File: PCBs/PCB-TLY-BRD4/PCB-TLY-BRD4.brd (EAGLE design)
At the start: 100 x 31 mm, 28 parts, among them IC1 ULN2803A, IC2 MCP23017SS

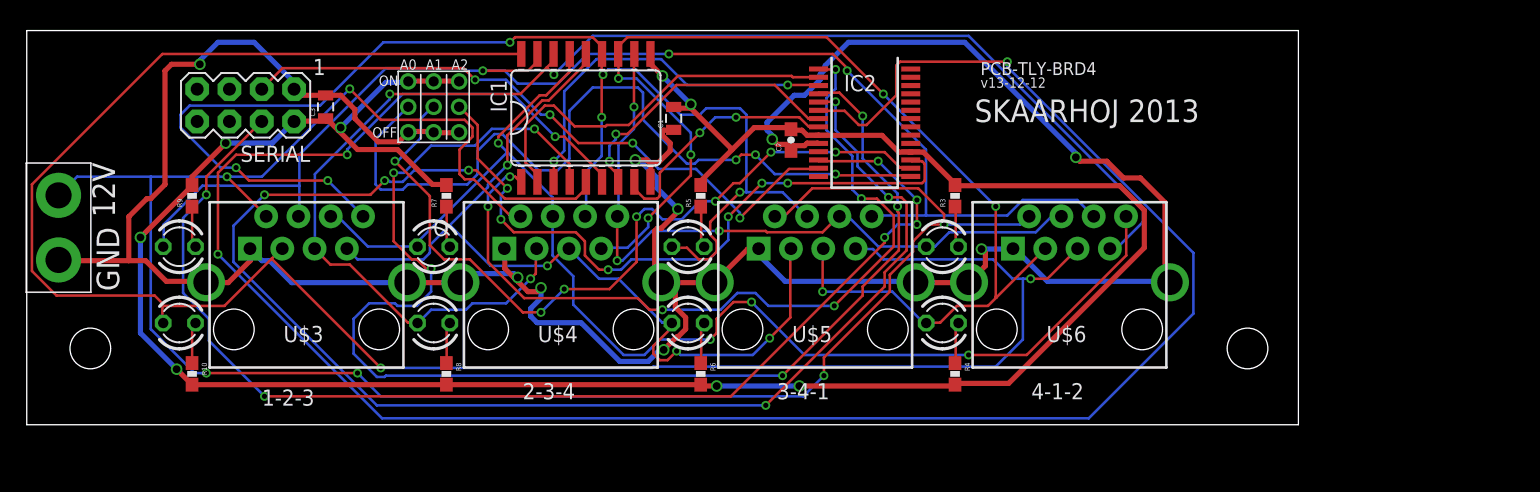
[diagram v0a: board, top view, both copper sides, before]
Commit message: Updated boards
Updated boards with logo before first sending to Alma.
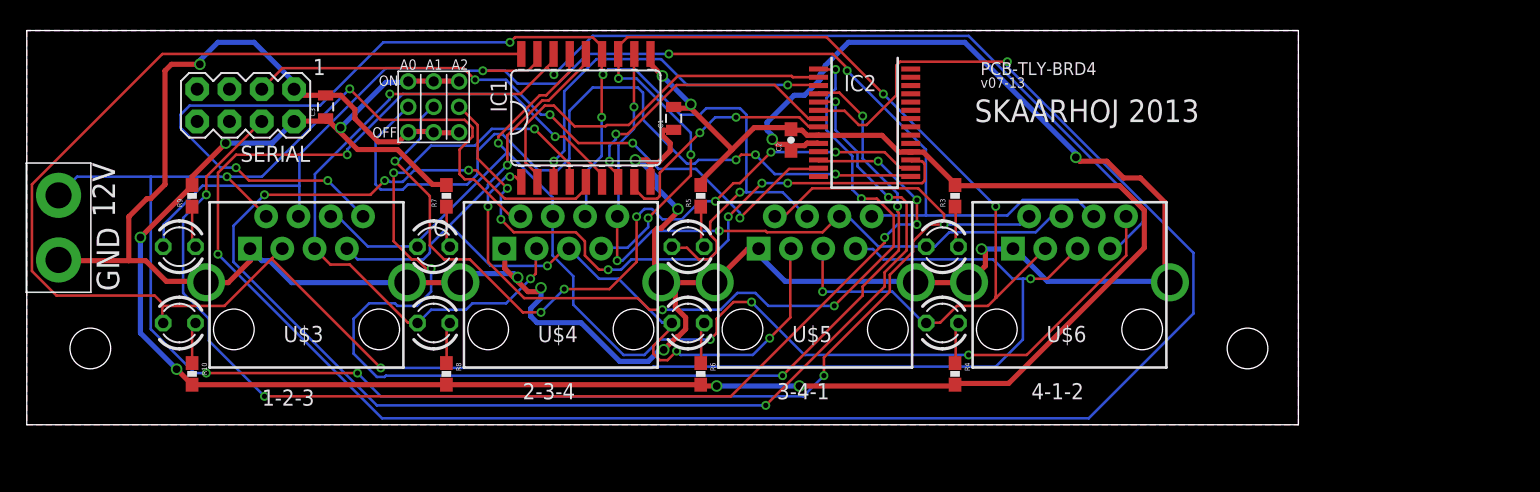
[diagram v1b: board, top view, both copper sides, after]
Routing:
- added copper zone on layer 1, net GND
- added copper zone on layer 16, net GND
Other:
- board text added: "v07-13"
- board text removed: "v13-12-12"

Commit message: Some new stuff
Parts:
- removed JP1: (no value), SparkFun:1X02_XTRA_BIG
- added J1: POWER_JACK_SMD, SKAARHOJ:POWER_JACK_SMD
- added U$15, U$20: GNDPAD6MM, SKAARHOJ:3.2MMPAD6MM
- added U$8, U$9: M08X2, SparkFun:2X8
- moved C3 68.0 mm to (91.5, 27.0)
- moved SERIAL 68.0 mm to (85.2, 27.1)
- moved U$19 44.0 mm to (76.0, 27.0)
- moved C2 42.8 mm to (102.4, 28.9), turned to 0 degrees
- moved IC2 37.9 mm to (103.8, 23.1), turned to 180 degrees
- moved IC1 1.84 mm to (42.1, 24.0), turned to 270 degrees
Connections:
- removed net N$34: IC1.2, IC2.2
- removed net N$35: IC1.3, IC2.3
- removed net N$36: IC1.4, IC2.4
- removed net N$37: IC1.5, IC2.5
- removed net N$38: IC1.6, IC2.6
- removed net N$39: IC1.7, IC2.7
- removed net N$40: IC1.8, IC2.8
- removed net N$5: IC1.1, IC2.1
- removed net N$82: JP1.2, U$3.2, U$4.2, U$5.2, U$6.2
- new net 12V: J1.PWR, U$3.2, U$4.2, U$5.2, U$6.2, U$8.15, U$9.15
- new net GPA0: IC2.21, U$8.2
- new net GPA1: IC2.22, U$8.4
- new net GPA2: IC2.23, U$8.6
- new net GPA3: IC2.24, U$8.8
- new net GPA4: IC2.25, U$8.10
- new net GPA5: IC2.26, U$8.12
- new net GPA6: IC2.27, U$8.14
- new net GPA7: IC2.28, U$8.16
- new net GPB0: IC1.1, IC2.1, U$9.2
- new net GPB1: IC1.2, IC2.2, U$9.4
- new net GPB2: IC1.3, IC2.3, U$9.6
- new net GPB3: IC1.4, IC2.4, U$9.8
- new net GPB4: IC1.5, IC2.5, U$9.10
- new net GPB5: IC1.6, IC2.6, U$9.12
- new net GPB6: IC1.7, IC2.7, U$9.14
- new net GPB7: IC1.8, IC2.8, U$9.16
- net 5V: now also U$8.13, U$9.13
- net GND: now also J1.GND, U$15.P$1, U$20.P$1, U$8.1, U$8.11, U$8.3, U$8.5, U$8.7, U$8.9, U$9.1, U$9.11, U$9.3, U$9.5, U$9.7, U$9.9; no longer JP1.1
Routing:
- net N$38: track 172.7 -> 0.00 mm, vias 4 -> 0
- net N$82: track 159.0 -> 0.00 mm, vias 6 -> 0
- net 12V: track 0.00 -> 156.7 mm, vias 0 -> 5
- net GPB0: track 0.00 -> 148.3 mm, vias 0 -> 8
- net GPB2: track 0.00 -> 138.9 mm, vias 0 -> 3
- net GPA7: track 0.00 -> 134.3 mm, vias 0 -> 3
- net GPA2: track 0.00 -> 128.2 mm, vias 0 -> 5
- net GPA4: track 0.00 -> 124.5 mm, vias 0 -> 1
- net GPA0: track 0.00 -> 124.0 mm, vias 0 -> 6
- net GPA5: track 0.00 -> 120.6 mm, vias 0 -> 6
- net GPA6: track 0.00 -> 119.9 mm, vias 0 -> 5
- net GPB7: track 0.00 -> 115.1 mm, vias 0 -> 5
- net GPA3: track 0.00 -> 114.8 mm, vias 0 -> 6
- net GPB4: track 0.00 -> 113.7 mm, vias 0 -> 5
- net N$37: track 113.5 -> 0.00 mm, vias 6 -> 0
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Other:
- board size 100 x 31 mm -> 117 x 31 mm
- board text removed: "12V"
- board text removed: "GND"

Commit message: Updates
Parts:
- added SJ1: SOLDERJUMPERNC2, SparkFun:SJ_2S-NOTRACE
- SERIAL: value M04X2 -> M04X2M2X4SMALLER; device SparkFun:2X4 -> SKAARHOJ:M2X4SMALLER
- U$19: value 3BITADDR -> 3BITADDRSMALL; device SKAARHOJ:3BITADDR -> SKAARHOJ:3BITADDR_SMALL
- moved U$19 2.00 mm to (74.0, 27.0)
- turned SERIAL to 270 degrees
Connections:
- removed net DISP_DATA_OUT: SERIAL.6
- removed net SLIDER_IN: SERIAL.5
- new net N$1: SERIAL.6, SJ1.1
- net 12V: now also SJ1.2
- net 5V: now also U$19.H0; no longer U$19.H3
- net A0: now also U$19.AS0
- net A1: now also U$19.AS1
- net A2: now also U$19.AS2
- net GND: now also U$19.L0; no longer U$19.L3
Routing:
- net GPA7: track 134.3 -> 170.2 mm
- net GPA1: track 112.4 -> 126.3 mm, vias 8 -> 10
- net 12V: track 156.7 -> 170.3 mm
- net N$1: track 0.00 -> 6.45 mm
- net A1: track 29.7 -> 33.7 mm
- net A2: track 27.6 -> 30.1 mm
- net GND: track 280.6 -> 282.4 mm, vias 8 -> 9
- net 5V: track 280.7 -> 282.5 mm, vias 10 -> 11
- net A0: track 30.7 -> 32.1 mm
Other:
- board text added: "PCB-TLY-BRD4, v03-16 SKAARHOJ 2016"
- board text removed: "1"
- board text removed: "PCB-TLY-BRD4"
- board text removed: "SKAARHOJ 2013"
- board text removed: "v07-13"
